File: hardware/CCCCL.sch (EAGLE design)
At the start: 11 parts, among them U1 LMV324

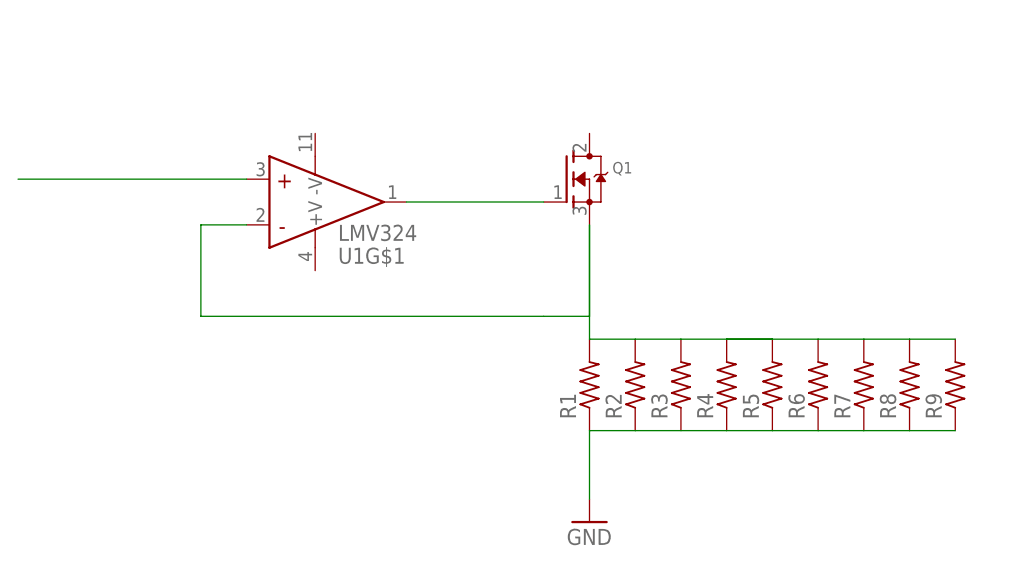
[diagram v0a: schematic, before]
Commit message: added the 10th resistor and battery power supply connection
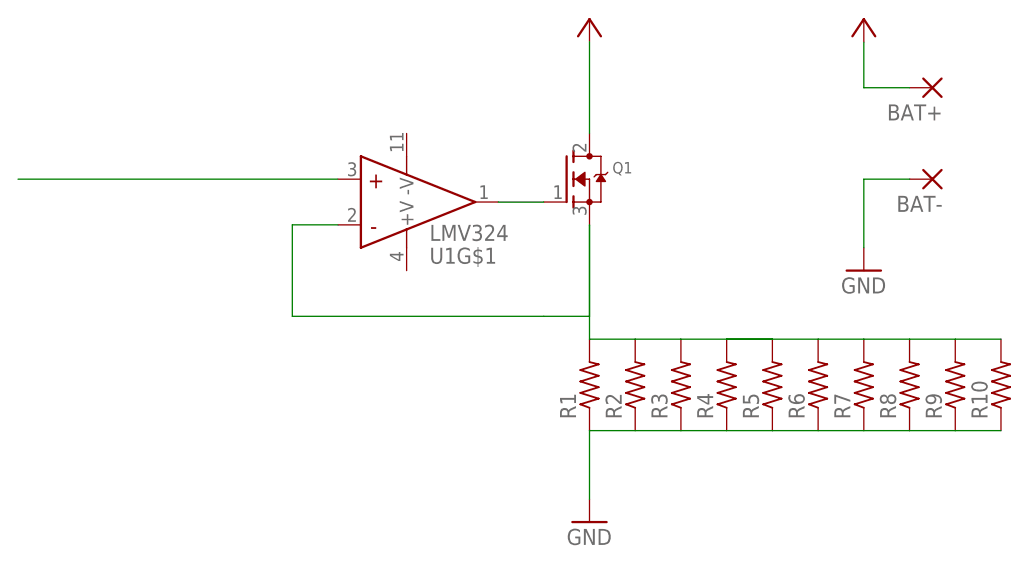
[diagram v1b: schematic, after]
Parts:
- added BAT+, BAT-: (no value), wirepad:3,17/1,3
- added R10: (no value), resistor:R-US_0309/12
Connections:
- new net +3V3: Q1.D
- new net VB: BAT+.P
- net GND: now also BAT-.P, R10.1
- net N$2: now also R10.2
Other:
- moved on the sheet: U1G$1
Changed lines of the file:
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@@
 <part name="R9" library="resistor" deviceset="R-US_" device="0309/12"/>
 <part name="GND1" library="supply1" deviceset="GND" device=""/>
+<part name="R10" library="resistor" deviceset="R-US_" device="0309/12"/>
+<part name="BAT+" library="wirepad" deviceset="3,17/1,3" device=""/>
+<part name="BAT-" library="wirepad" deviceset="3,17/1,3" device=""/>
+<part name="GND2" library="supply1" deviceset="GND" device=""/>
+<part name="VB" library="supply1" deviceset="+3V3" device=""/>
+<part name="VB1" library="supply1" deviceset="+3V3" device=""/>
 </parts>
 <sheets>
@@
 </plain>
 <instances>
-<instance part="U1" gate="G$1" x="30.48" y="58.42" rot="MR180"/>
+<instance part="U1" gate="G$1" x="40.64" y="58.42" rot="MR180"/>
 <instance part="Q1" gate="G$1" x="63.5" y="60.96"/>
 <instance part="R1" gate="G$1" x="66.04" y="38.1" rot="R90"/>
@@
 <instance part="R9" gate="G$1" x="106.68" y="38.1" rot="R90"/>
 <instance part="GND1" gate="1" x="66.04" y="22.86"/>
+<instance part="R10" gate="G$1" x="111.76" y="38.1" rot="R90"/>
+<instance part="BAT+" gate="1" x="104.14" y="71.12" rot="R180"/>
+<instance part="BAT-" gate="1" x="104.14" y="60.96" rot="R180"/>
+<instance part="GND2" gate="1" x="96.52" y="50.8"/>
+<instance part="VB" gate="G$1" x="96.52" y="78.74" smashed="yes"/>
+<instance part="VB1" gate="G$1" x="66.04" y="78.74" smashed="yes"/>
 </instances>
 <busses>
@@
 <pinref part="U1" gate="G$1" pin="OUT"/>
 <pinref part="Q1" gate="G$1" pin="G"/>
-<wire x1="45.72" y1="58.42" x2="60.96" y2="58.42" width="0.1524" layer="91"/>
+<wire x1="55.88" y1="58.42" x2="60.96" y2="58.42" width="0.1524" layer="91"/>
 </segment>
 </net>
@@
 <segment>
 <pinref part="U1" gate="G$1" pin="-IN"/>
-<wire x1="27.94" y1="55.88" x2="22.86" y2="55.88" width="0.1524" layer="91"/>
-<wire x1="22.86" y1="55.88" x2="22.86" y2="45.72" width="0.1524" layer="91"/>
-<wire x1="22.86" y1="45.72" x2="60.96" y2="45.72" width="0.1524" layer="91"/>
+<wire x1="38.1" y1="55.88" x2="33.02" y2="55.88" width="0.1524" layer="91"/>
+<wire x1="33.02" y1="55.88" x2="33.02" y2="45.72" width="0.1524" layer="91"/>
+<wire x1="33.02" y1="45.72" x2="60.96" y2="45.72" width="0.1524" layer="91"/>
 <pinref part="Q1" gate="G$1" pin="S"/>
 <wire x1="60.96" y1="45.72" x2="66.04" y2="45.72" width="0.1524" layer="91"/>
@@
 <wire x1="101.6" y1="43.18" x2="106.68" y2="43.18" width="0.1524" layer="91"/>
 <wire x1="66.04" y1="55.88" x2="66.04" y2="43.18" width="0.1524" layer="91"/>
+<pinref part="R10" gate="G$1" pin="2"/>
+<wire x1="106.68" y1="43.18" x2="111.76" y2="43.18" width="0.1524" layer="91"/>
 </segment>
 </net>
@@
 <wire x1="66.04" y1="33.02" x2="66.04" y2="25.4" width="0.1524" layer="91"/>
 <pinref part="GND1" gate="1" pin="GND"/>
+<pinref part="R10" gate="G$1" pin="1"/>
+<wire x1="111.76" y1="33.02" x2="106.68" y2="33.02" width="0.1524" layer="91"/>
+</segment>
+<segment>
+<pinref part="BAT-" gate="1" pin="P"/>
+<wire x1="101.6" y1="60.96" x2="96.52" y2="60.96" width="0.1524" layer="91"/>
+<pinref part="GND2" gate="1" pin="GND"/>
+<wire x1="96.52" y1="60.96" x2="96.52" y2="53.34" width="0.1524" layer="91"/>
 </segment>
 </net>
@@
 <segment>
 <pinref part="U1" gate="G$1" pin="+IN"/>
-<wire x1="27.94" y1="60.96" x2="2.54" y2="60.96" width="0.1524" layer="91"/>
+<wire x1="38.1" y1="60.96" x2="2.54" y2="60.96" width="0.1524" layer="91"/>
 </segment>
 </net>
+<net name="VB" class="0">
+<segment>
+<pinref part="BAT+" gate="1" pin="P"/>
+<wire x1="101.6" y1="71.12" x2="96.52" y2="71.12" width="0.1524" layer="91"/>
+<wire x1="96.52" y1="71.12" x2="96.52" y2="76.2" width="0.1524" layer="91"/>
+<pinref part="VB" gate="G$1" pin="+3V3"/>
+</segment>
+</net>
+<net name="+3V3" class="0">
+<segment>
+<pinref part="Q1" gate="G$1" pin="D"/>
+<wire x1="66.04" y1="66.04" x2="66.04" y2="76.2" width="0.1524" layer="91"/>
+<pinref part="VB1" gate="G$1" pin="+3V3"/>
+</segment>
+</net>

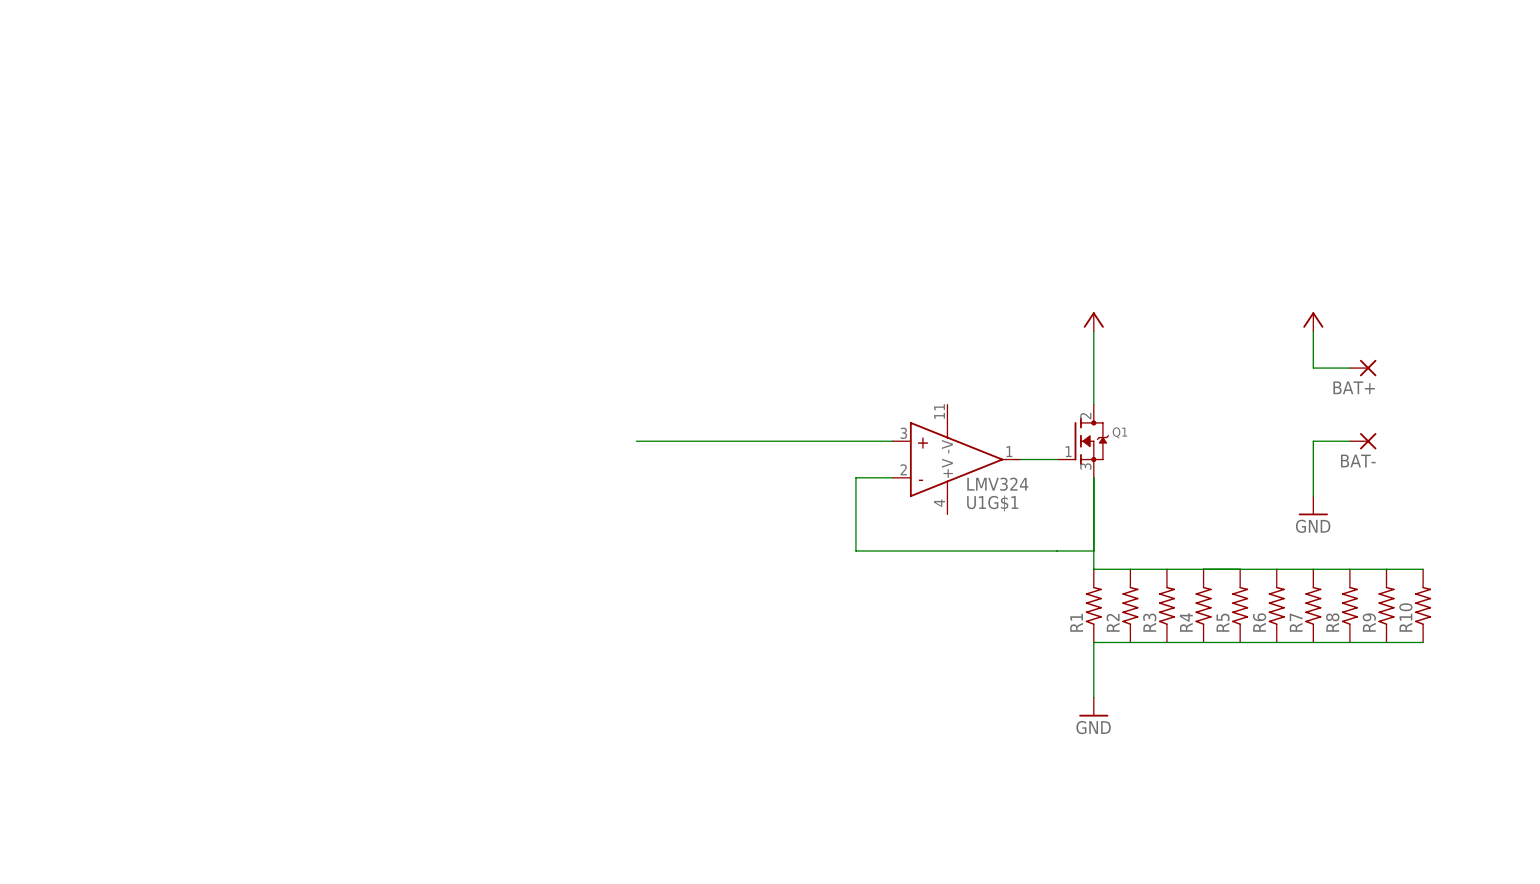
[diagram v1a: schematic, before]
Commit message: added a tiny85 uC for controll
added uC and ISP, LPF for both PWM gen and feedback compensation
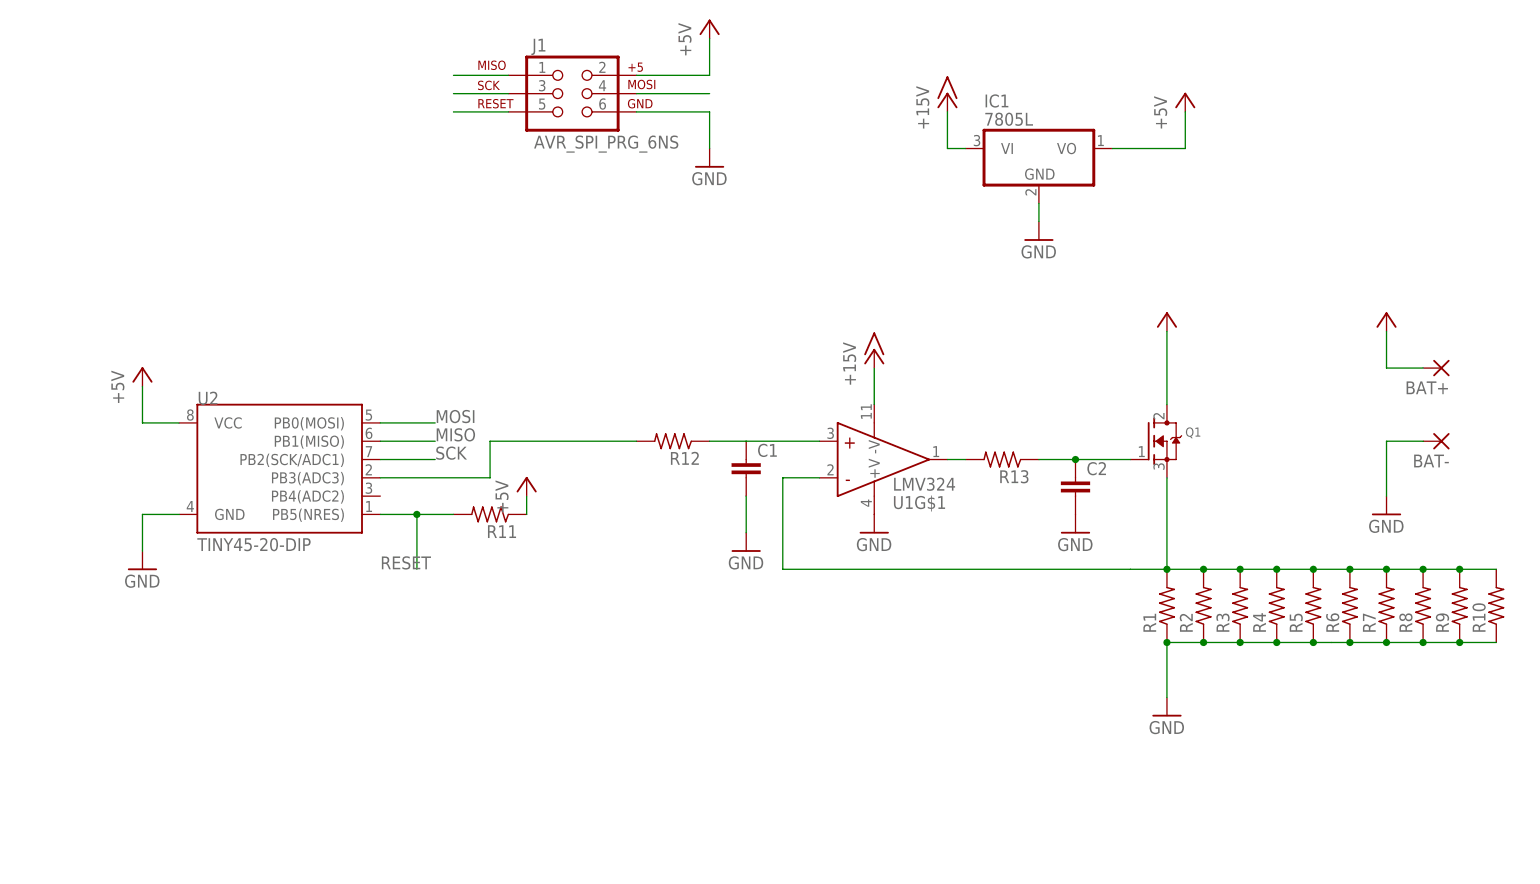
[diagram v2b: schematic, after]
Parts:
- added C1, C2: (no value), rcl:C-EU025-040X050
- added IC1: 7805L, adafruit:7805L
- added J1: AVR_SPI_PRG_6NS, SparkFun-Connectors:AVR_SPI_PRG_6NS
- added R11, R12, R13: (no value), resistor:R-US_0309/12
- added U2: TINY45-20-DIP, SparkFun-DigitalIC:ATTINY45TINY45-20-DIP
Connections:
- new net +15V: IC1.VI, U1G$1.-V
- new net +5V: J1.2, R11.1, U2.VCC
- new net MISO: J1.1, U2.PB1(MISO)
- new net MOSI: J1.4, U2.PB0(MOSI)
- new net N$4: C1.1, R12.1, U1G$1.+IN
- new net N$5: C2.1, Q1.G, R13.1
- new net RESET: J1.5, R11.2, U2.PB5(NRES)
- new net SCK: J1.3, U2.PB2(SCK/ADC1)
- net GND: now also C1.2, C2.2, IC1.GND, J1.6, U1G$1.+V, U2.GND
- net N$1: now also R13.2; no longer Q1.G
- net N$3: now also R12.2, U2.PB3(ADC3); no longer U1G$1.+IN
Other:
- moved on the sheet: BAT+, BAT-, Q1, R1, R10, R2, R3, R4, R5, R6, R7, R8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

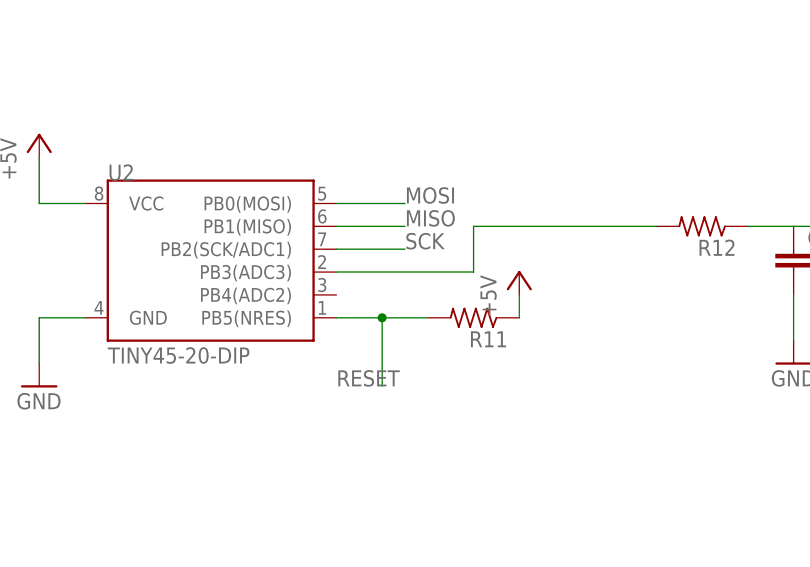
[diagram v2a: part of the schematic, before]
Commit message: changed PWM pin for output to analog
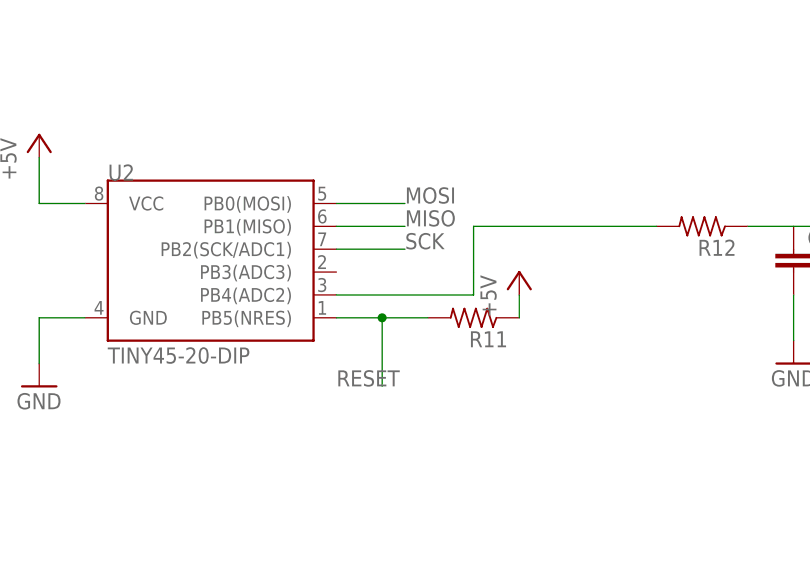
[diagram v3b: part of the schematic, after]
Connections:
- net N$3: now also U2.PB4(ADC2); no longer U2.PB3(ADC3)
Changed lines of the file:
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@@
 <net name="N$3" class="0">
 <segment>
-<pinref part="U2" gate="G$1" pin="PB3(ADC3)"/>
-<wire x1="-33.02" y1="55.88" x2="-17.78" y2="55.88" width="0.1524" layer="91"/>
 <wire x1="-17.78" y1="55.88" x2="-17.78" y2="60.96" width="0.1524" layer="91"/>
 <wire x1="-17.78" y1="60.96" x2="2.54" y2="60.96" width="0.1524" layer="91"/>
 <pinref part="R12" gate="G$1" pin="2"/>
+<pinref part="U2" gate="G$1" pin="PB4(ADC2)"/>
+<wire x1="-33.02" y1="53.34" x2="-17.78" y2="53.34" width="0.1524" layer="91"/>
+<wire x1="-17.78" y1="53.34" x2="-17.78" y2="55.88" width="0.1524" layer="91"/>
 </segment>
 </net>

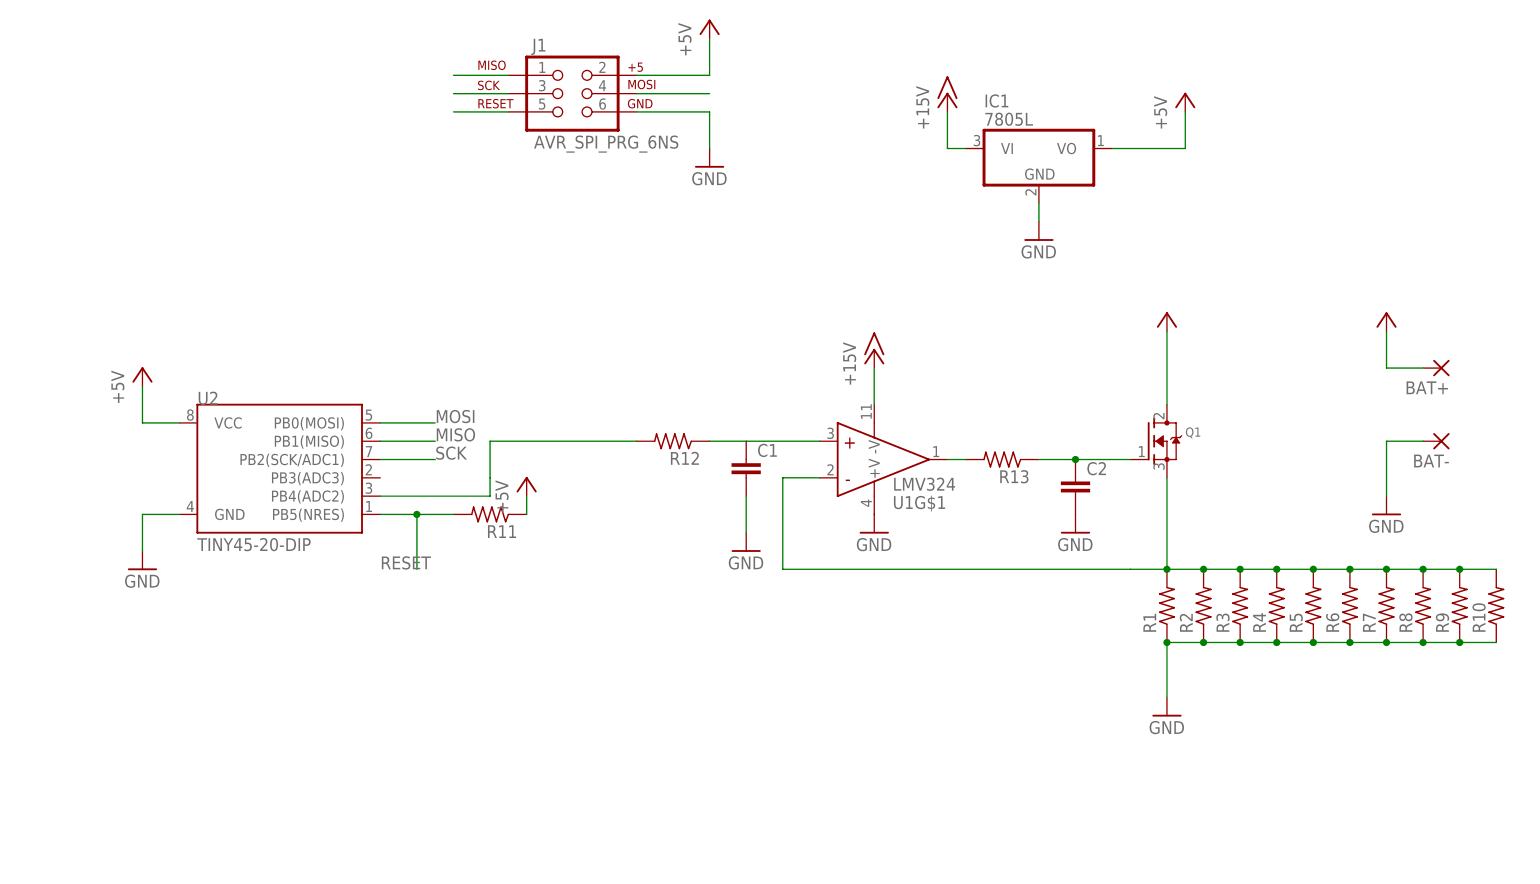
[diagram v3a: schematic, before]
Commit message: innitial commit for tiny261 added USB circuit
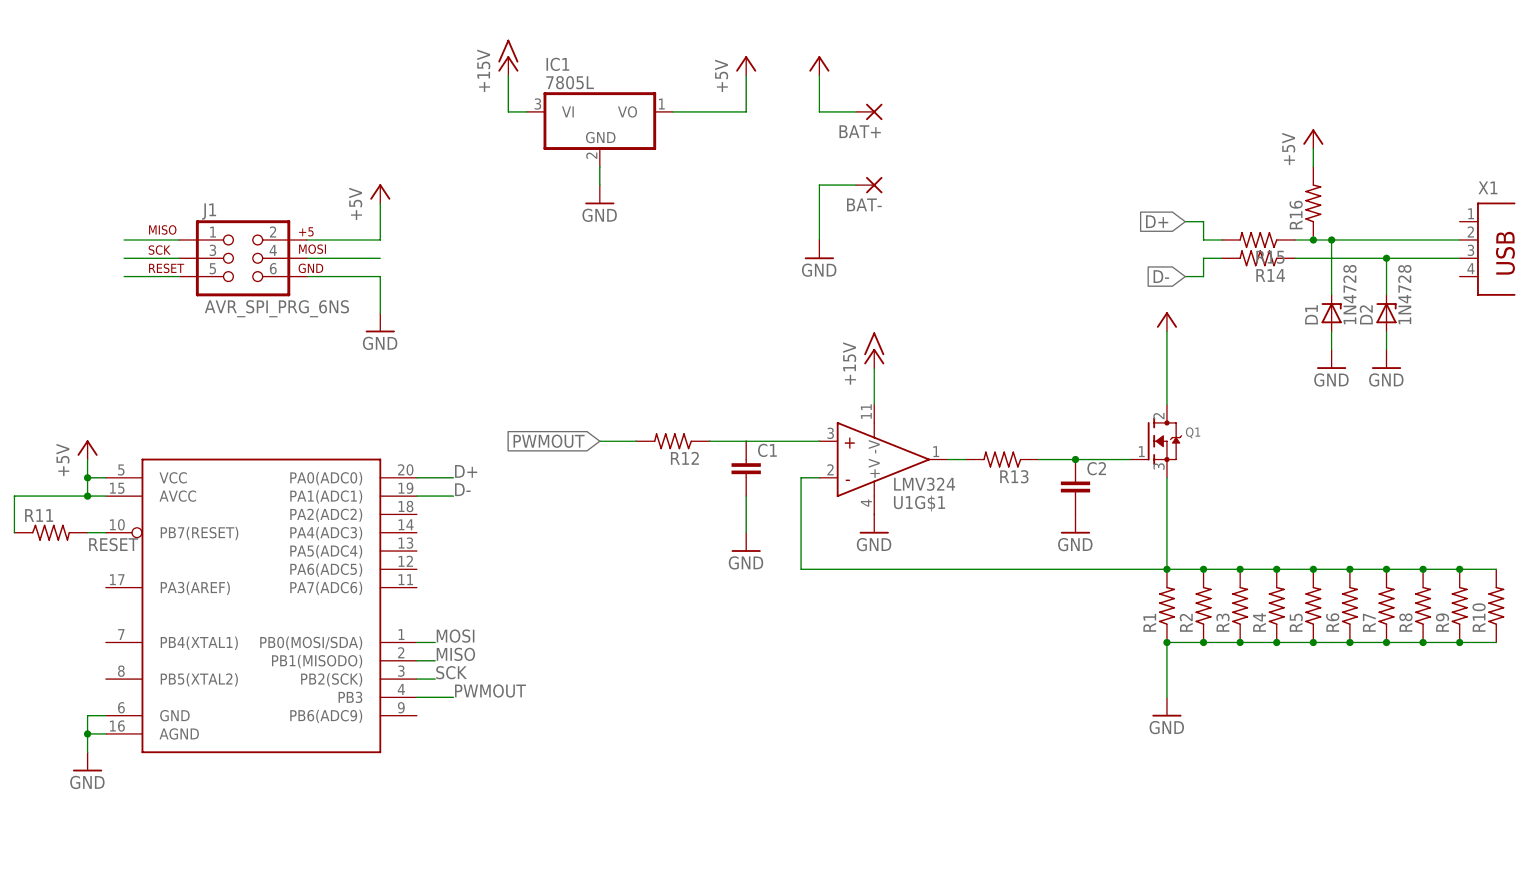
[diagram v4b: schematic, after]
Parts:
- removed U2: TINY45-20-DIP, SparkFun-DigitalIC:ATTINY45TINY45-20-DIP
- added D1, D2: 1N4728, diode:1N4728
- added R14, R15, R16: (no value), resistor:R-US_0309/12
- added U$1: ATTINY261ADIP, EVT-Eagle-Library:ATTINY261ADIP
- added X1: (no value), con-berg:PN87520
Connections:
- new net D+: R15.2, U$1.PA0(ADC0)
- new net D-: R14.2, U$1.PA1(ADC1)
- new net N$6: D1.C, R15.1, R16.1, X1.2
- new net PWMOUT: R12.2, U$1.PB3
- net +5V: now also IC1.VO, R16.2, U$1.AVCC, U$1.VCC; no longer U2.VCC
- net GND: now also D1.A, D2.A, U$1.AGND, U$1.GND; no longer U2.GND
- net MISO: now also U$1.PB1(MISODO); no longer U2.PB1(MISO)
- net MOSI: now also U$1.PB0(MOSI/SDA); no longer U2.PB0(MOSI)
- net N$3: now also D2.C, R14.1, X1.3; no longer R12.2, U2.PB4(ADC2)
- net RESET: now also U$1.PB7(RESET); no longer U2.PB5(NRES)
- net SCK: now also U$1.PB2(SCK); no longer U2.PB2(SCK/ADC1)
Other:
- moved on the sheet: BAT+, BAT-, IC1, J1, R11
